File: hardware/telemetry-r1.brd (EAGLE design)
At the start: 63.5 x 63.5 mm, 101 parts, among them IC1 COPERNICUSSMD, IC10 TPS70933, IC2 TPS70933, IC3 74HC137, IC4 STM32L073CZT6, IC5 TPS62160, IC6 HX1, IC7 LMP7702, IC8 ADXL345, IC9 HIH9131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

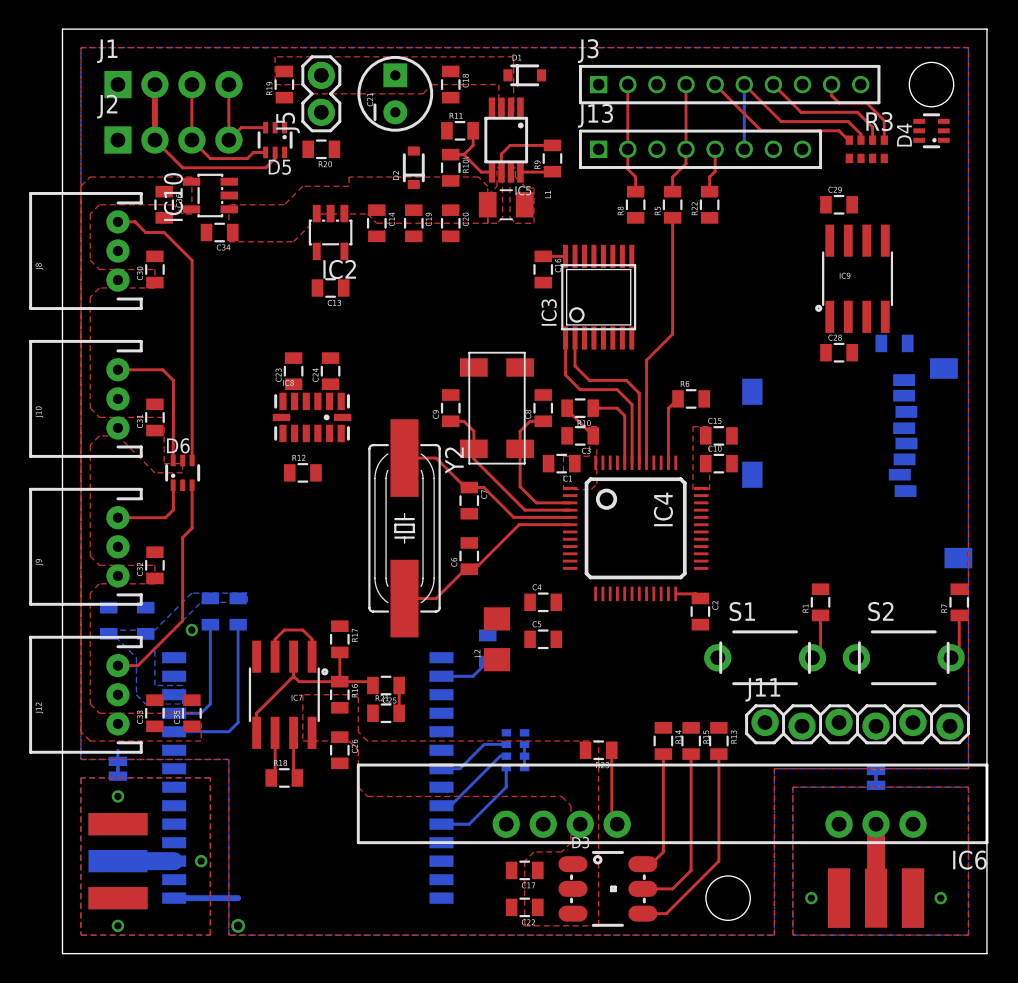
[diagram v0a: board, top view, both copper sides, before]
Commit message: Fully route telemtery PCB, please review
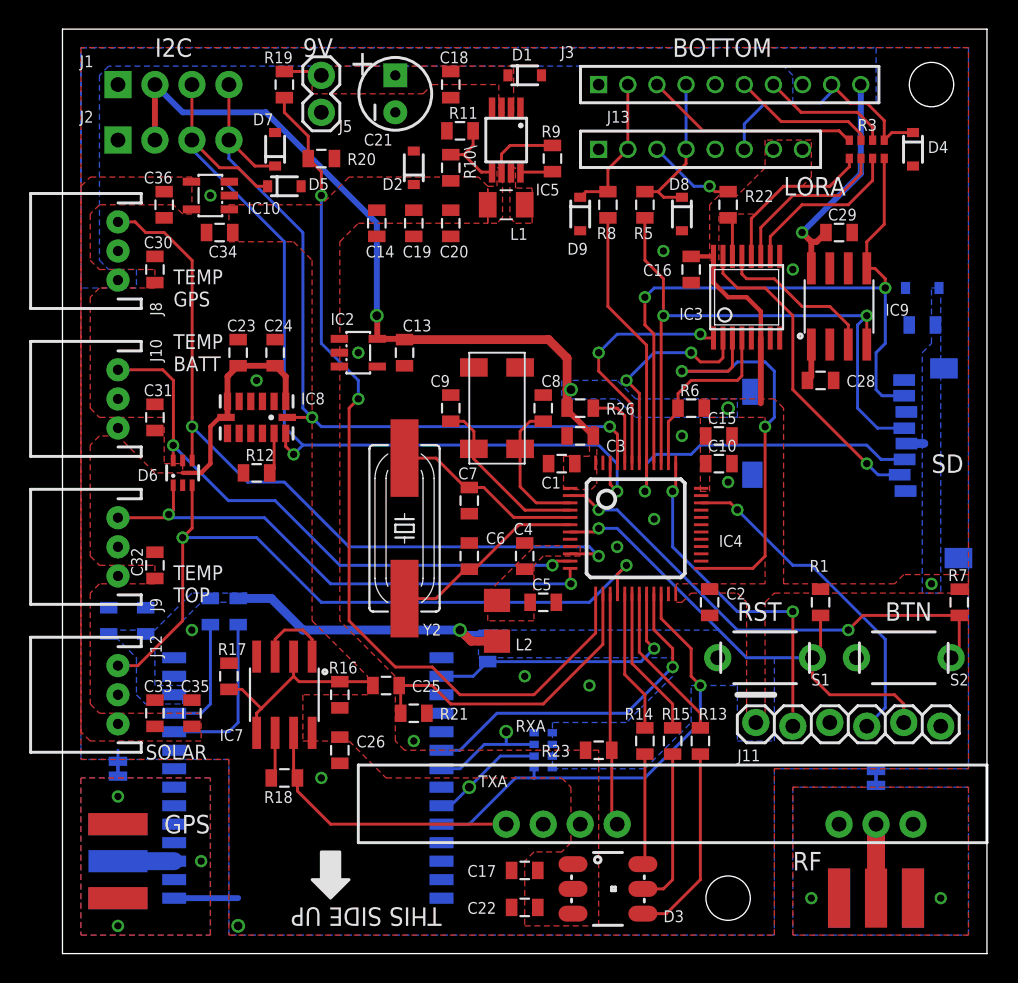
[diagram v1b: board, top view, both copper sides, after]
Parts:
- added D10, D7, D8, D9: 5.6V, SparkFun-DiscreteSemi:SOD-323
- added U$2: (no value), HAB:GARAGE
- added U$5: (no value), HAB:SWIFT
- D4, D5: value CM1213A -> 5.6V; device HAB:SC70-6L -> SparkFun-DiscreteSemi:SOD-323
- moved IC3 10.2 mm to (47.0, 45.1)
- moved C16 10.2 mm to (43.2, 47.0)
- moved IC2 8.47 mm to (20.3, 41.3), turned to 270 degrees
- moved R17 8.03 mm to (11.4, 19.1)
- moved C13 6.75 mm to (23.5, 41.3), turned to 270 degrees
- moved C23 4.02 mm to (12.1, 41.3)
- moved C24 4.02 mm to (14.6, 41.3)
- moved IC8 3.81 mm to (13.3, 36.8)
- moved C4 3.42 mm to (31.8, 27.3), turned to 90 degrees
- moved D5 3.24 mm to (15.2, 52.7), turned to 0 degrees
- moved R12 3.18 mm to (13.3, 33.0)
- moved C5 2.54 mm to (33.0, 24.1)
- moved C27 2.29 mm to (59.1, 43.2)
- moved C28 2.29 mm to (52.1, 39.4)
- moved IC9 2.29 mm to (53.3, 44.5)
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- renumbered R10 to R26
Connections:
- net !RST!: no longer J13.7
- net 3.3V: now also D10.C, J13.7; no longer D4.5, D5.5
- net B_CSADC: now also J3.7, R3.2; no longer D4.4, J3.9, R3.1
- net B_CSHUM: now also J3.3; no longer D4.3, J3.5
- net B_CSPRS: now also J3.6, R3.3; no longer D4.6, J3.7, R3.2
- net B_LORA: now also J13.3; no longer J13.5
- net B_MISO: now also D4.C, J3.9, R3.1; no longer D4.1, J3.6, R3.3
- net B_MOSI: now also D9.C, J13.2, J3.2, R8.2; no longer D5.1, J13.4, J3.4, R5.2
- net B_SCK: now also D8.C, J13.4, J3.4, R5.2; no longer D5.6, J13.2, J3.2, R8.2
- net CSADC: now also R3.7; no longer R3.8
- net CSPRS: now also R3.6; no longer R3.7
- net GND: now also D10.A, D4.A, D5.A, D7.A, D8.A, D9.A, J13.5, J3.5; no longer D4.2, D5.2, J13.3, J3.3
- net MISO: now also R3.8; no longer R3.6
- net MOSI: now also R8.1; no longer R5.1
- net SCK: now also R5.1; no longer R8.1
- net SCL: now also D7.C; no longer D5.3
- net SDA: now also D5.C; no longer D5.4
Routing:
- net 3.3V: track 21.2 -> 86.8 mm, vias 0 -> 5
- net VDIV: track 0.00 -> 61.8 mm, vias 0 -> 2
- net SDA: track 9.58 -> 63.2 mm, vias 0 -> 2
- net MISO: track 0.00 -> 48.0 mm, vias 0 -> 2
- net SCL: track 6.69 -> 54.3 mm, vias 0 -> 2
- net SCK: track 0.00 -> 43.8 mm, vias 0 -> 2
- net INSOL: track 15.3 -> 50.9 mm, vias 0 -> 2
- net TEMPG: track 19.9 -> 53.6 mm, vias 0 -> 2
- net VS: track 0.00 -> 31.0 mm, vias 0 -> 1
- net BTN: track 3.14 -> 34.1 mm, vias 0 -> 2
- net TEMPB: track 9.61 -> 40.4 mm, vias 0 -> 2
- net TEMPH: track 5.73 -> 36.4 mm, vias 0 -> 2
- net CSA2: track 0.00 -> 30.2 mm, vias 0 -> 2
- net !RST!: track 3.14 -> 33.2 mm, vias 0 -> 1
- net GPSRX: track 6.84 -> 31.3 mm, vias 0 -> 1
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- added copper zone on layer 1, net VDDA
- added copper zone on layer 16, net VS
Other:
- board text added: "+"
- board text added: "9V"
- board text added: "BOTTOM"
- board text added: "BTN"
- board text added: "Contact ~STCARLSO 301 956 5041"
- board text added: "GPS"
- board text added: "HAB Project"
- board text added: "I2C"
- board text added: "LORA"
- board text added: "Microsoft Maker Garage"
- board text added: "PROGRAM"
- board text added: "RF"
- board text added: "RST"
- board text added: "RXA"
- board text added: "SD"
- board text added: "SOLAR"
- board text added: "TEMP BATT"
- board text added: "TEMP GPS"
- board text added: "TEMP TOP"
- board text added: "THIS SIDE UP"
- board text added: "TXA"
- board text added: "Telemetry Rev 3"

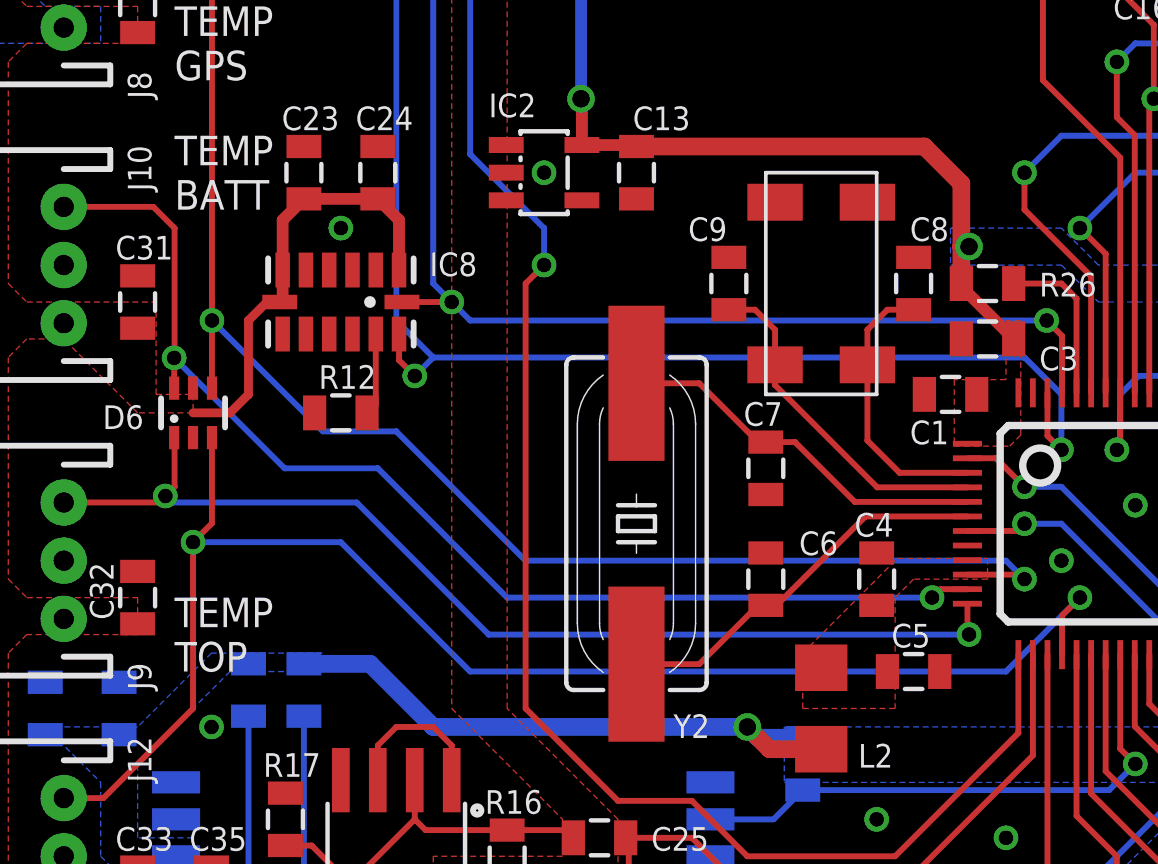
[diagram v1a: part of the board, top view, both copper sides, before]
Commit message: Fix a few issues on the telemetry PCB. Add schematic (no layout) for bottom/sensors board.
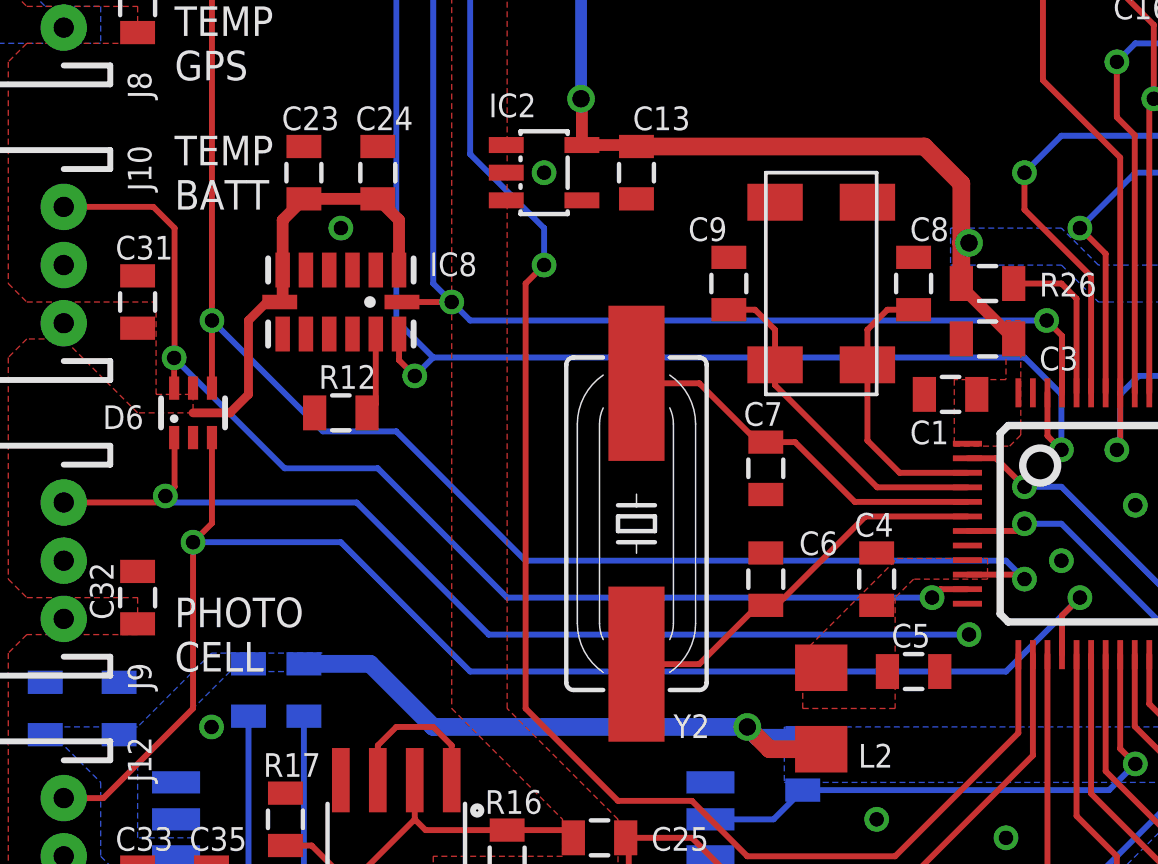
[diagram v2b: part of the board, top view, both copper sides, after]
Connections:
- new net PHOTO: IC4.12
- net TEMPH: no longer IC4.12
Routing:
- net TEMPH: track 36.4 -> 35.4 mm
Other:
- board text added: "PHOTO CELL"
- board text removed: "TEMP TOP"
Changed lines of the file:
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@@
 <?xml version="1.0" encoding="utf-8"?>
 <!DOCTYPE eagle SYSTEM "eagle.dtd">
-<eagle version="7.4.0">
+<eagle version="7.6.0">
 <drawing>
 <settings>
@@
 <text x="7.62" y="44.45" size="1.016" layer="21" font="vector" ratio="10">TEMP
 GPS</text>
-<text x="7.62" y="24.13" size="1.016" layer="21" font="vector" ratio="10">TEMP
-TOP</text>
+<text x="7.62" y="24.13" size="1.016" layer="21" font="vector" ratio="10">PHOTO
+CELL</text>
 <text x="7.62" y="40.005" size="1.016" layer="21" font="vector" ratio="10">TEMP
 BATT</text>
@@
 <wire x1="28.07" y1="21.46" x2="27.305" y2="22.225" width="0.6096" layer="1"/>
 <wire x1="57.972296875" y1="35.036575" x2="59.166575" y2="35.036575" width="0.6096" layer="16"/>
-<wire x1="34.66" y1="37.465" x2="34.66" y2="38.735" width="0.6096" layer="1"/>
-<wire x1="34.66" y1="38.735" x2="34.66" y2="40.905" width="0.6096" layer="1"/>
+<wire x1="34.66" y1="37.465" x2="34.66" y2="38.862" width="0.6096" layer="1"/>
+<wire x1="34.66" y1="38.862" x2="34.66" y2="40.905" width="0.6096" layer="1"/>
 <wire x1="34.66" y1="40.905" x2="33.39" y2="42.175" width="0.6096" layer="1"/>
 <wire x1="23.495" y1="42.175" x2="33.39" y2="42.175" width="0.6096" layer="1"/>
@@
 <contactref element="D10" pad="C"/>
 <via x="45.72" y="37.465" extent="1-16" drill="0.6"/>
-<via x="34.925" y="38.735" extent="1-16" drill="0.6"/>
-<wire x1="34.925" y1="38.735" x2="34.66" y2="38.735" width="0.6096" layer="1"/>
+<via x="34.925" y="38.862" extent="1-16" drill="0.6"/>
+<wire x1="34.925" y1="38.862" x2="34.66" y2="38.862" width="0.6096" layer="1"/>
 <polygon width="0.2032" layer="16" isolate="0.2032" rank="2">
 <vertex x="34.29" y="39.37"/>
@@
 <contactref element="J9" pad="3"/>
 <contactref element="D6" pad="1"/>
-<contactref element="IC4" pad="12"/>
 <wire x1="3.81" y1="29.94" x2="7.08" y2="29.94" width="0.2032" layer="1"/>
 <wire x1="7.08" y1="29.94" x2="7.3025" y2="30.1625" width="0.2032" layer="1"/>
@@
 <via x="7.3025" y="30.1625" extent="1-16" drill="0.5"/>
 <wire x1="7.3025" y1="30.1625" x2="7.62" y2="30.48" width="0.2032" layer="1"/>
-<wire x1="34.87" y1="26.46" x2="34.87" y2="25.455" width="0.2032" layer="1"/>
 <wire x1="34.87" y1="25.455" x2="34.925" y2="25.4" width="0.2032" layer="1"/>
 </signal>
@@
 <wire x1="43.37" y1="52.705" x2="40.83" y2="55.245" width="0.2032" layer="16"/>
 </signal>
+<signal name="PHOTO">
+<contactref element="IC4" pad="12"/>
+</signal>
 </signals>

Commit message: Update telemetry board to include Pavel's new LPF
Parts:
- added C37, C39: 100p, SparkFun-Passives:0805
- added C38: 47n, SparkFun-Passives:0805
- added R10: 18K, SparkFun-Passives:0805
- added R27: 330k, SparkFun-Passives:0805
- added R28: 10K, SparkFun-Passives:0805
- C25: value 100p -> 330p
- R16: value 1.5M -> 470K
- R17: value 470K -> 220K
- R18: value 100 -> 10K
- R21: value DNP -> 680
- moved R21 13.0 mm to (15.2, 26.0), turned to 90 degrees
- moved R18 8.91 mm to (14.6, 21.0)
- moved R17 7.62 mm to (19.1, 19.1)
- moved C26 2.54 mm to (19.1, 11.4)
- moved IC7 2.54 mm to (15.2, 15.2)
- moved R16 2.54 mm to (19.1, 15.2)
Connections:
- removed net A2O: IC7.1, IC7.3
- new net LP-: IC7.6, R28.1
- new net LP1: C37.1, IC7.1, R18.2, R21.1
- new net LP2: C38.1, R21.2, R27.1
- new net LP3: C39.1, IC7.5, R27.2
- net A+: no longer IC7.5
- net A-: now also C37.2, IC7.3, R10.2; no longer IC7.6
- net DAC: no longer R21.2
- net GND: now also C38.2, C39.2, R10.1; no longer R21.1
- net TXD: now also R28.2; no longer R18.2
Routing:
- net LP2: track 0.00 -> 13.7 mm
- net LP3: track 0.00 -> 9.04 mm
- net LP1: track 0.00 -> 8.07 mm
- net A+: track 14.8 -> 9.07 mm
- net A2O: track 5.45 -> 0.00 mm
- net A-: track 3.21 -> 7.17 mm
- net LP-: track 0.00 -> 2.57 mm
- net DAC: track 21.6 -> 19.8 mm
- net TXD: track 19.4 -> 18.0 mm
- net GND: vias 15 -> 16
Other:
- board text added: "PHOTO CELL 1"
- board text added: "PHOTO CELL 2"
- board text removed: "PHOTO CELL"
- board text removed: "SOLAR"

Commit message: Fix broken photocell routing
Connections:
- removed net TEMPH: D6.1, J9.3
- net PHOTO: now also D6.1, J9.3
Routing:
- net PHOTO: track 0.00 -> 36.4 mm, vias 0 -> 2
- net TEMPH: track 35.4 -> 0.00 mm, vias 2 -> 0
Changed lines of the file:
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@@
 <wire x1="33.625" y1="53.68" x2="33.655" y2="53.71" width="0.2032" layer="1"/>
-</signal>
-<signal name="TEMPH">
-<contactref element="J9" pad="3"/>
-<contactref element="D6" pad="1"/>
-<wire x1="3.81" y1="29.94" x2="7.08" y2="29.94" width="0.2032" layer="1"/>
-<wire x1="7.08" y1="29.94" x2="7.3025" y2="30.1625" width="0.2032" layer="1"/>
-<wire x1="7.62" y1="30.48" x2="7.62" y2="32.155" width="0.2032" layer="1"/>
-<wire x1="7.62" y1="32.155" x2="7.605" y2="32.17" width="0.2032" layer="1"/>
-<via x="34.925" y="25.4" extent="1-16" drill="0.5"/>
-<wire x1="34.925" y1="25.4" x2="18.415" y2="25.4" width="0.2032" layer="16"/>
-<wire x1="18.415" y1="25.4" x2="13.875" y2="29.94" width="0.2032" layer="16"/>
-<wire x1="13.875" y1="29.94" x2="7.525" y2="29.94" width="0.2032" layer="16"/>
-<wire x1="7.525" y1="29.94" x2="7.3025" y2="30.1625" width="0.2032" layer="16"/>
-<via x="7.3025" y="30.1625" extent="1-16" drill="0.5"/>
-<wire x1="7.3025" y1="30.1625" x2="7.62" y2="30.48" width="0.2032" layer="1"/>
-<wire x1="34.87" y1="25.455" x2="34.925" y2="25.4" width="0.2032" layer="1"/>
 </signal>
 <signal name="HXEN">
@@
 <signal name="PHOTO">
 <contactref element="IC4" pad="12"/>
+<contactref element="J9" pad="3"/>
+<contactref element="D6" pad="1"/>
+<wire x1="7.62" y1="30.48" x2="7.62" y2="32.155" width="0.2032" layer="1"/>
+<wire x1="7.62" y1="32.155" x2="7.605" y2="32.17" width="0.2032" layer="1"/>
+<via x="34.925" y="25.4" extent="1-16" drill="0.5"/>
+<wire x1="34.925" y1="25.4" x2="18.415" y2="25.4" width="0.2032" layer="16"/>
+<wire x1="18.415" y1="25.4" x2="13.875" y2="29.94" width="0.2032" layer="16"/>
+<wire x1="13.875" y1="29.94" x2="7.525" y2="29.94" width="0.2032" layer="16"/>
+<wire x1="7.525" y1="29.94" x2="7.3025" y2="30.1625" width="0.2032" layer="16"/>
+<via x="7.3025" y="30.1625" extent="1-16" drill="0.5"/>
+<wire x1="7.3025" y1="30.1625" x2="7.62" y2="30.48" width="0.2032" layer="1"/>
+<wire x1="34.87" y1="25.455" x2="34.925" y2="25.4" width="0.2032" layer="1"/>
+<wire x1="34.87" y1="25.455" x2="34.87" y2="26.46" width="0.2032" layer="1"/>
+<wire x1="3.81" y1="29.94" x2="7.08" y2="29.94" width="0.2032" layer="1"/>
+<wire x1="7.08" y1="29.94" x2="7.3025" y2="30.1625" width="0.2032" layer="1"/>
 </signal>
 <signal name="LP1">
